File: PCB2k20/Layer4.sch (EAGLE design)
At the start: 57 parts, among them J1 CONN_03, J2 CONN_03

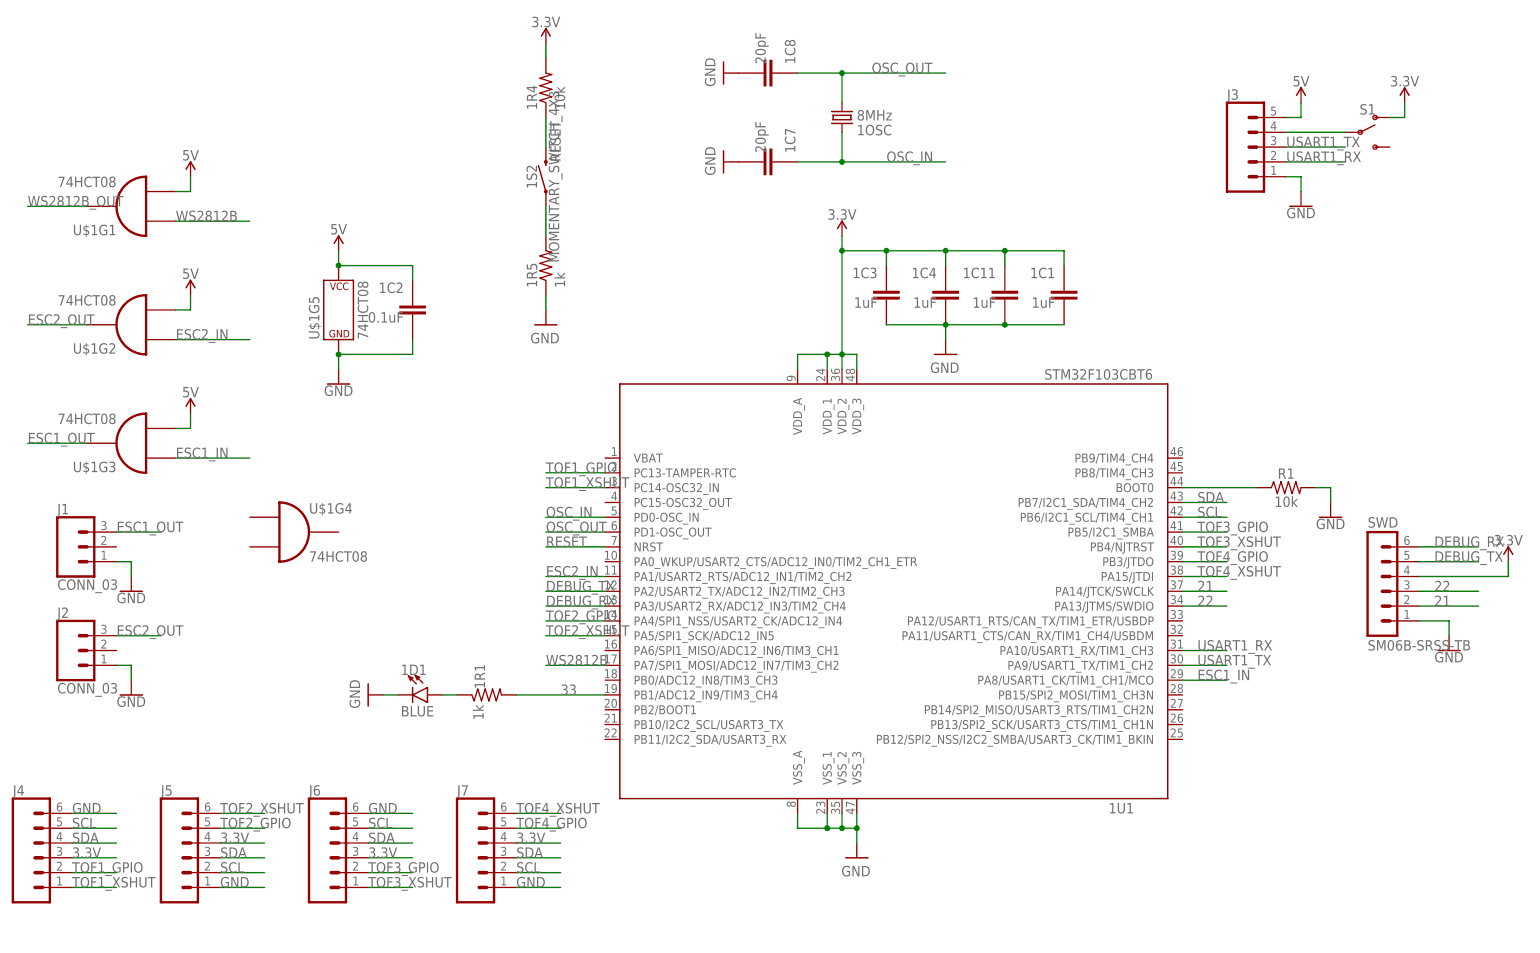
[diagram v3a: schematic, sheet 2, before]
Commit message: BROKEN VERSION for 3d models
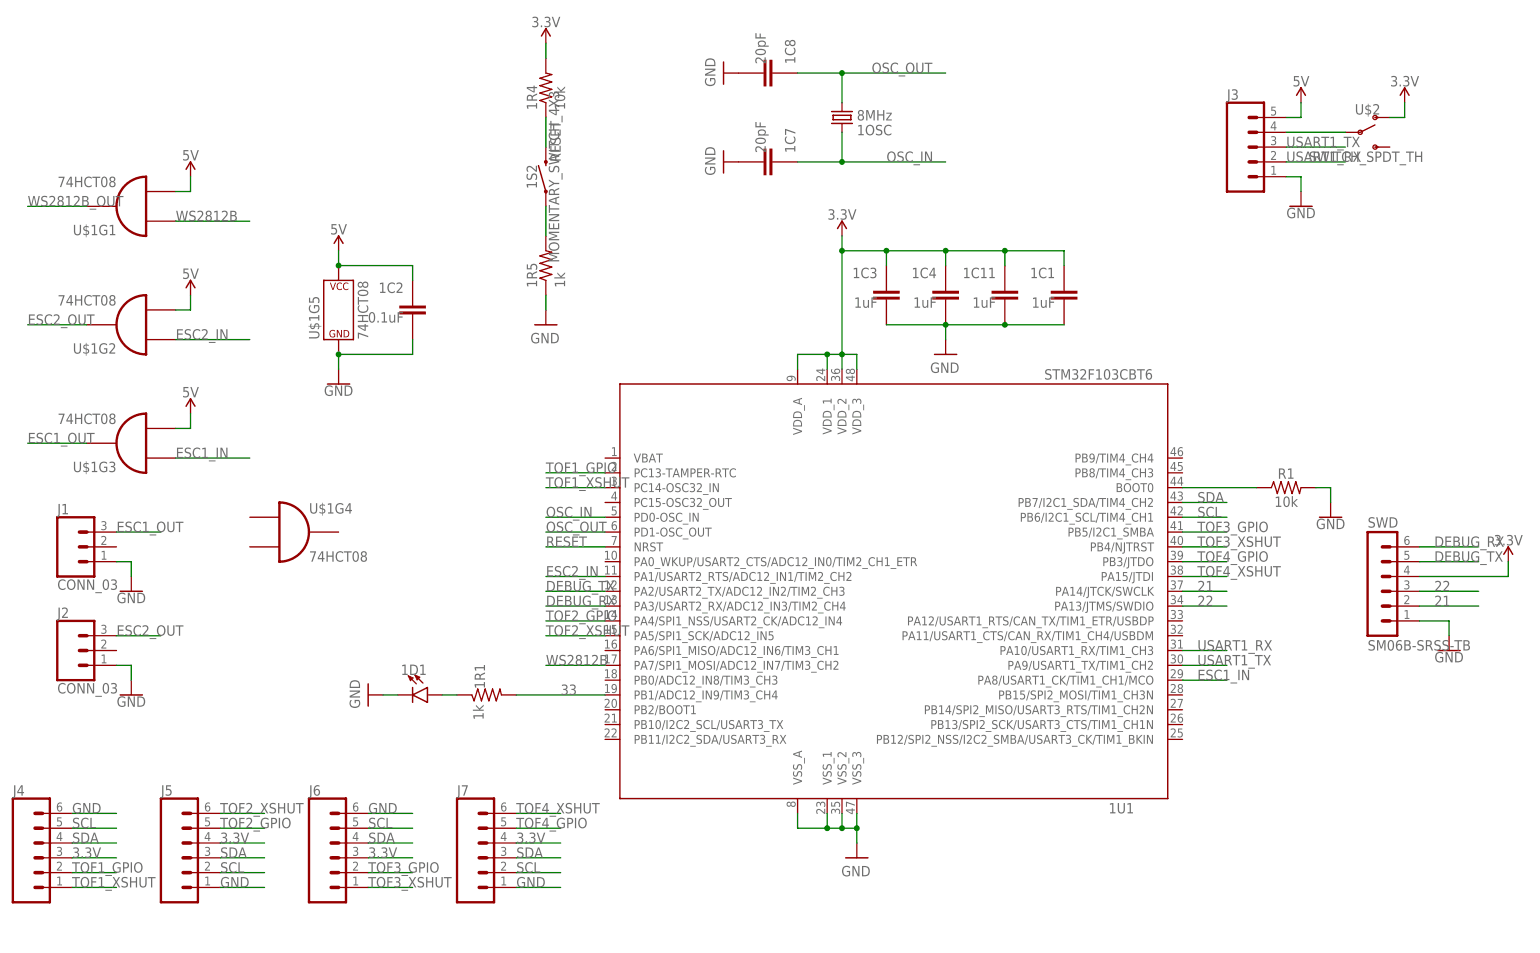
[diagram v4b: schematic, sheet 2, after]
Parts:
- removed S1: (no value), SparkFun-Switches:SWITCH-SPDT-PTH-11.6X4.0MM-LOCK
- added U$2: SWITCH_SPDT_TH, JH:SWITCH_SPDT_TH
- 1D1: device SparkFun-LED:LED-BLUE0603 -> JH:LED0603
- 1OSC: device SparkFun-Clocks:CRYSTALSMD-5X3.2-2PAD -> JH:CRYSTAL_5032
- J3: device SparkFun-Connectors:CONN_05LOCK -> Connectors:CONN_05LOCK
- J4, J5, J6, J7: device SparkFun-Connectors:CONN_06LOCK -> Connectors:CONN_06LOCK
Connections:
- net 3.3V: now also U$2.O; no longer S1.O
- net N$26: now also U$2.P; no longer S1.P
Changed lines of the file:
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@@
 <?xml version="1.0" encoding="utf-8"?>
 <!DOCTYPE eagle SYSTEM "eagle.dtd">
-<eagle version="9.5.2">
+<eagle version="9.6.1">
 <drawing>
 <settings>
@@
 <part name="1R5" library="JH" library_urn="urn:adsk.eagle:library:6027132" deviceset="RESISTOR" device="0603" package3d_urn="urn:adsk.eagle:package:15441228/3" value="1k"/>
 <part name="SUPPLY17" library="SparkFun-PowerSymbols" library_urn="urn:adsk.eagle:library:530" deviceset="GND" device="" value="GND"/>
-<part name="1OSC" library="SparkFun-Clocks" library_urn="urn:adsk.eagle:library:511" deviceset="CRYSTAL" device="SMD-5X3.2-2PAD" package3d_urn="urn:adsk.eagle:package:37520/1" value="8MHz"/>
+<part name="1OSC" library="JH" library_urn="urn:adsk.eagle:library:6027132" deviceset="CRYSTAL" device="_5032" package3d_urn="urn:adsk.eagle:package:19858037/2" value="8MHz"/>
 <part name="FRAME2" library="SparkFun-Aesthetics" library_urn="urn:adsk.eagle:library:507" deviceset="FRAME-A4L" device=""/>
 <part name="SWD" library="con-JST SH" library_urn="urn:adsk.eagle:library:17006044" deviceset="SM06B-SRSS" device="-TB" package3d_urn="urn:adsk.eagle:package:17006117/1"/>
 <part name="GND5" library="SparkFun-PowerSymbols" library_urn="urn:adsk.eagle:library:530" deviceset="GND" device=""/>
 <part name="1S2" library="JH" library_urn="urn:adsk.eagle:library:6027132" deviceset="MOMENTARY_SWITCH_4X3" device="" package3d_urn="urn:adsk.eagle:package:16673543/1"/>
-<part name="1D1" library="SparkFun-LED" library_urn="urn:adsk.eagle:library:529" deviceset="LED-BLUE" device="0603" package3d_urn="urn:adsk.eagle:package:39354/1" value="BLUE"/>
+<part name="1D1" library="JH" library_urn="urn:adsk.eagle:library:6027132" deviceset="LED" device="0603" package3d_urn="urn:adsk.eagle:package:19858044/2" value="BLUE"/>
 <part name="1C11" library="JH" library_urn="urn:adsk.eagle:library:6027132" deviceset="CAPACITOR" device="0603" package3d_urn="urn:adsk.eagle:package:15441226/3" value="1uF"/>
 <part name="SUPPLY1" library="SparkFun-PowerSymbols" library_urn="urn:adsk.eagle:library:530" deviceset="3.3V" device=""/>
@@
 <part name="GND16" library="SparkFun-PowerSymbols" library_urn="urn:adsk.eagle:library:530" deviceset="GND" device=""/>
 <part name="GND17" library="SparkFun-PowerSymbols" library_urn="urn:adsk.eagle:library:530" deviceset="GND" device=""/>
-<part name="U$1" library="JH" library_urn="urn:adsk.eagle:library:6027132" deviceset="74HCT08" device="" package3d_urn="urn:adsk.eagle:package:9157825/1"/>
+<part name="U$1" library="JH" library_urn="urn:adsk.eagle:library:6027132" deviceset="74HCT08" device="" package3d_urn="urn:adsk.eagle:package:9157825/2"/>
 <part name="J1" library="JH" library_urn="urn:adsk.eagle:library:6027132" deviceset="CONN_03" device="" package3d_urn="urn:adsk.eagle:package:15924798/2"/>
 <part name="J2" library="JH" library_urn="urn:adsk.eagle:library:6027132" deviceset="CONN_03" device="" package3d_urn="urn:adsk.eagle:package:15924798/2"/>
@@
 <part name="GND19" library="SparkFun-PowerSymbols" library_urn="urn:adsk.eagle:library:530" deviceset="GND" device=""/>
 <part name="GND20" library="SparkFun-PowerSymbols" library_urn="urn:adsk.eagle:library:530" deviceset="GND" device=""/>
-<part name="J3" library="SparkFun-Connectors" library_urn="urn:adsk.eagle:library:513" deviceset="CONN_05" device="LOCK" package3d_urn="urn:adsk.eagle:package:38105/1"/>
+<part name="J3" library="Connectors" library_urn="urn:adsk.eagle:library:19813715" deviceset="CONN_05" device="LOCK" package3d_urn="urn:adsk.eagle:package:19813887/2"/>
 <part name="SUPPLY30" library="SparkFun-PowerSymbols" library_urn="urn:adsk.eagle:library:530" deviceset="3.3V" device=""/>
 <part name="SUPPLY31" library="SparkFun-PowerSymbols" library_urn="urn:adsk.eagle:library:530" deviceset="5V" device=""/>
@@
 <part name="C15" library="JH" library_urn="urn:adsk.eagle:library:6027132" deviceset="CAPACITOR" device="0603" package3d_urn="urn:adsk.eagle:package:15441226/3" value="0.1uF"/>
 <part name="AC8" library="JH" library_urn="urn:adsk.eagle:library:6027132" deviceset="CAPACITOR" device="0603" package3d_urn="urn:adsk.eagle:package:15441226/3" value="0.1uF"/>
-<part name="J4" library="SparkFun-Connectors" library_urn="urn:adsk.eagle:library:513" deviceset="CONN_06" device="LOCK" package3d_urn="urn:adsk.eagle:package:38002/1"/>
-<part name="J5" library="SparkFun-Connectors" library_urn="urn:adsk.eagle:library:513" deviceset="CONN_06" device="LOCK" package3d_urn="urn:adsk.eagle:package:38002/1"/>
-<part name="J6" library="SparkFun-Connectors" library_urn="urn:adsk.eagle:library:513" deviceset="CONN_06" device="LOCK" package3d_urn="urn:adsk.eagle:package:38002/1"/>
-<part name="J7" library="SparkFun-Connectors" library_urn="urn:adsk.eagle:library:513" deviceset="CONN_06" device="LOCK" package3d_urn="urn:adsk.eagle:package:38002/1"/>
+<part name="J4" library="Connectors" library_urn="urn:adsk.eagle:library:19813715" deviceset="CONN_06" device="LOCK" package3d_urn="urn:adsk.eagle:package:19813917/2"/>
+<part name="J5" library="Connectors" library_urn="urn:adsk.eagle:library:19813715" deviceset="CONN_06" device="LOCK" package3d_urn="urn:adsk.eagle:package:19813917/2"/>
+<part name="J6" library="Connectors" library_urn="urn:adsk.eagle:library:19813715" deviceset="CONN_06" device="LOCK" package3d_urn="urn:adsk.eagle:package:19813917/2"/>
+<part name="J7" library="Connectors" library_urn="urn:adsk.eagle:library:19813715" deviceset="CONN_06" device="LOCK" package3d_urn="urn:adsk.eagle:package:19813917/2"/>
 <part name="1C1" library="JH" library_urn="urn:adsk.eagle:library:6027132" deviceset="CAPACITOR" device="0603" package3d_urn="urn:adsk.eagle:package:15441226/3" value="1uF"/>
 <part name="1C2" library="JH" library_urn="urn:adsk.eagle:library:6027132" deviceset="CAPACITOR" device="0603" package3d_urn="urn:adsk.eagle:package:15441226/3" value="0.1uF"/>
@@
 <part name="SUPPLY27" library="SparkFun-PowerSymbols" library_urn="urn:adsk.eagle:library:530" deviceset="5V" device=""/>
 <part name="SUPPLY32" library="SparkFun-PowerSymbols" library_urn="urn:adsk.eagle:library:530" deviceset="5V" device=""/>
-<part name="S1" library="SparkFun-Switches" library_urn="urn:adsk.eagle:library:535" deviceset="SWITCH-SPDT" device="-PTH-11.6X4.0MM-LOCK" package3d_urn="urn:adsk.eagle:package:40181/1"/>
+<part name="U$2" library="JH" library_urn="urn:adsk.eagle:library:6027132" deviceset="SWITCH_SPDT" device="_TH" package3d_urn="urn:adsk.eagle:package:19858057/2"/>
 </parts>
 <sheets>
@@
 <instance part="1D1" gate="G$1" x="83.82" y="63.5" smashed="yes" rot="R270">
 <attribute name="NAME" x="79.248" y="66.929" size="1.778" layer="95" font="vector"/>
-<attribute name="VALUE" x="79.248" y="61.595" size="1.778" layer="96" font="vector" align="top-left"/>
 </instance>
 <instance part="1C11" gate="G$1" x="182.88" y="132.08" smashed="yes" rot="MR0">
@@
 <attribute name="VALUE" x="79.756" y="127.381" size="1.778" layer="96" rot="MR0"/>
 </instance>
-<instance part="S1" gate="1" x="243.84" y="160.02" smashed="yes">
+<instance part="U$2" gate="G$1" x="243.84" y="160.02" smashed="yes">
 <attribute name="NAME" x="245.11" y="163.068" size="1.778" layer="95" font="vector" align="bottom-center"/>
 <attribute name="VALUE" x="244.856" y="156.718" size="1.778" layer="96" font="vector" align="top-center"/>
@@
 </segment>
 <segment>
-<pinref part="S1" gate="1" pin="O"/>
 <pinref part="SUPPLY30" gate="G$1" pin="3.3V"/>
 <wire x1="248.92" y1="162.56" x2="251.46" y2="162.56" width="0.1524" layer="91"/>
 <wire x1="251.46" y1="162.56" x2="251.46" y2="165.1" width="0.1524" layer="91"/>
+<pinref part="U$2" gate="G$1" pin="O"/>
 </segment>
 </net>
@@
 <pinref part="J3" gate="G$1" pin="4"/>
 <wire x1="231.14" y1="160.02" x2="241.3" y2="160.02" width="0.1524" layer="91"/>
-<pinref part="S1" gate="1" pin="P"/>
-</segment>
-</net>
+<pinref part="U$2" gate="G$1" pin="P"/>
+</segment>
+</net>
